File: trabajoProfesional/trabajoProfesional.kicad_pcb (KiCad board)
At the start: 2 copper layers, 190.8 x 81 mm, 115 parts, among them IC1 TS51231-QFNR, Q1 BSS84, U1 1501

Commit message: Editado el footprint que no teniamos, completando las ultimas placas
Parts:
- removed SensorPresion1: MS583730BA01-50, Connector_PinHeader_1.00mm:PinHeader_2x02_P1.00mm_Vertical_SMD
- removed U1: 1501, Connector_PinHeader_1.00mm:PinHeader_2x05_P1.00mm_Vertical_SMD
- added 4M0: 1501, Connector_PinHeader_2.54mm:PinHeader_2x05_P2.54mm_Vertical_SMD, F.Cu at (203.0, 117.8)
- added 4MS: MS583730BA01-50, Connector_PinHeader_2.54mm:PinHeader_2x02_P2.54mm_Vertical_SMD, B.Cu at (208.4, 112.4)
-  : renamed from TS80002; value Conn_01x20_Male -> 6TS8
- moved C11 59.2 mm to (-20.7, 109.5)
- moved Reset1 59.2 mm to (-6.29, 108.5)
- moved SDA1 59.2 mm to (-6.79, 114.0)
- moved TXCoil1 59.2 mm to (-12.3, 114.5)
- moved TXCoil2 59.2 mm to (-12.3, 108.5)
- moved C17 50.2 mm to (30.9, 154.4), turned to 180 degrees
- moved C16 28.1 mm to (30.1, 125.8), turned to 270 degrees
- moved C19 27.7 mm to (95.3, 109.6)
- moved R4 27.7 mm to (95.3, 112.5)
- moved C12 24.4 mm to (37.5, 122.2), turned to 270 degrees
- moved C18 23.6 mm to (40.6, 118.7), turned to 90 degrees
- moved C15 23.1 mm to (43.5, 123.0), turned to 90 degrees
- moved C10 23.0 mm to (33.3, 142.0)
- moved IC1 23.0 mm to (30.6, 148.8)
- moved R8 23.0 mm to (40.6, 125.8), turned to 270 degrees
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- renumbered Cin1 to 1C1, Cbst1 to 1C10, Cs2 to 1C2, Cout4 to 1C3, Cout3 to 1C4, Cc2 to 1C5, Cin2 to 1C6, Cc1 to 1C7, Cout1 to 1C8, Cout2 to 1C9, Coil1 to 1Coil1, Coil2 to 1Coil2, Lout1 to 1L1, R2fb1 to 1R1, Rmod_cfg1 to 1R2, R1fb1 to 1R3, RecpetorPotenciaInalambrica1 to 1RP, AdministracionBateria1 to 2AB, BatPositivo1 to 2B+, Cbat1 to 2C1, Cvin1 to 2C2, 3CH to 2CH, opt1 to 2D1, DbyPass1 to 2D2, batGND1 to 2GND, Q1 to 2Q1, RIPRGM1 to 2R1, Rstatus1 to 2R2, Riso_pd1 to 2R3, 3Vin to 2Vin, 3Vo to 2Vo, C4 to 3C1, C5 to 3C2, C2 to 3C3, C1 to 3C4, C3 to 3C5, D4 to 3D1, D1 to 3D2, D3 to 3D3, D2 to 3D4, DriverPotencia1 to 3DP, HV+1 to 3HV+, HV-1 to 3HV-, PiezoElectrico1 to 3PE, 2SN to 3SN, 10V1 to 3V10, 2Vin to 3Vin, C6 to 4C1, R1 to 4R1, R2 to 4R2, AlertDONE1 to 6Alert, Debug1 to 6Dg, SCL1 to 6SCL, Vcc5V1 to 6V5
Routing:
- net SDAPresion: track 23.1 -> 31.9 mm
- net SCLPresion: track 37.4 -> 28.7 mm
- net Net-(C6-Pad2): track 47.3 -> 38.9 mm
- net GND: track 387.3 -> 389.5 mm
- net /Bateria/Cargando: track 39.9 -> 42.1 mm
- net /Salida/SN1ONOFF: track 28.2 -> 26.6 mm
- net /Salida/SP1ONOFF: track 17.6 -> 18.4 mm
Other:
- outline, holes or cut-outs redrawn
- net class PIstasAnchas added: clearance 0.025, trace_width 1, via_dia 0.8, via_drill 0.4

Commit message: "placa 6 casi completa"
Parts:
- 6Alert, 6Dg, 6SCL, 6V5: moved to B.Cu
- moved 6Alert 14.7 mm to (41.4, 114.7)
- moved R5 14.1 mm to (67.1, 116.1), turned to 270 degrees
- moved 6SCL 8.85 mm to (49.9, 126.4)
- moved 6Dg 7.91 mm to (62.6, 117.4)
- moved 6V5 5.80 mm to (30.8, 114.2)
- moved C8 5.22 mm to (66.2, 109.1)
- moved D5 3.81 mm to (61.7, 111.7)
- moved C9 3.43 mm to (60.2, 107.2), turned to 0 degrees
- moved R6 2.78 mm to (56.3, 114.5)
- moved C13 2.48 mm to (54.4, 107.2)
- moved R7 2.37 mm to (56.3, 111.0)
- moved R3 0.92 mm to (60.2, 117.9)
- moved   0.82 mm to (49.4, 118.4)
- moved C7 0.75 mm to (49.0, 111.3)
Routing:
- net Net-(C13-Pad1): track 0.00 -> 17.3 mm
- net Net-(C8-Pad1): track 0.00 -> 14.3 mm
- net Net-(C7-Pad1): track 0.00 -> 12.7 mm
- net Net-(Debug1-Pad1): track 0.00 -> 11.8 mm, vias 0 -> 1
- net Net-(IC1-Pad1): track 0.00 -> 9.44 mm
- net Net-(SCL1-Pad1): track 0.00 -> 6.69 mm, vias 0 -> 1
- net Net-(C8-Pad2): track 0.00 -> 6.05 mm

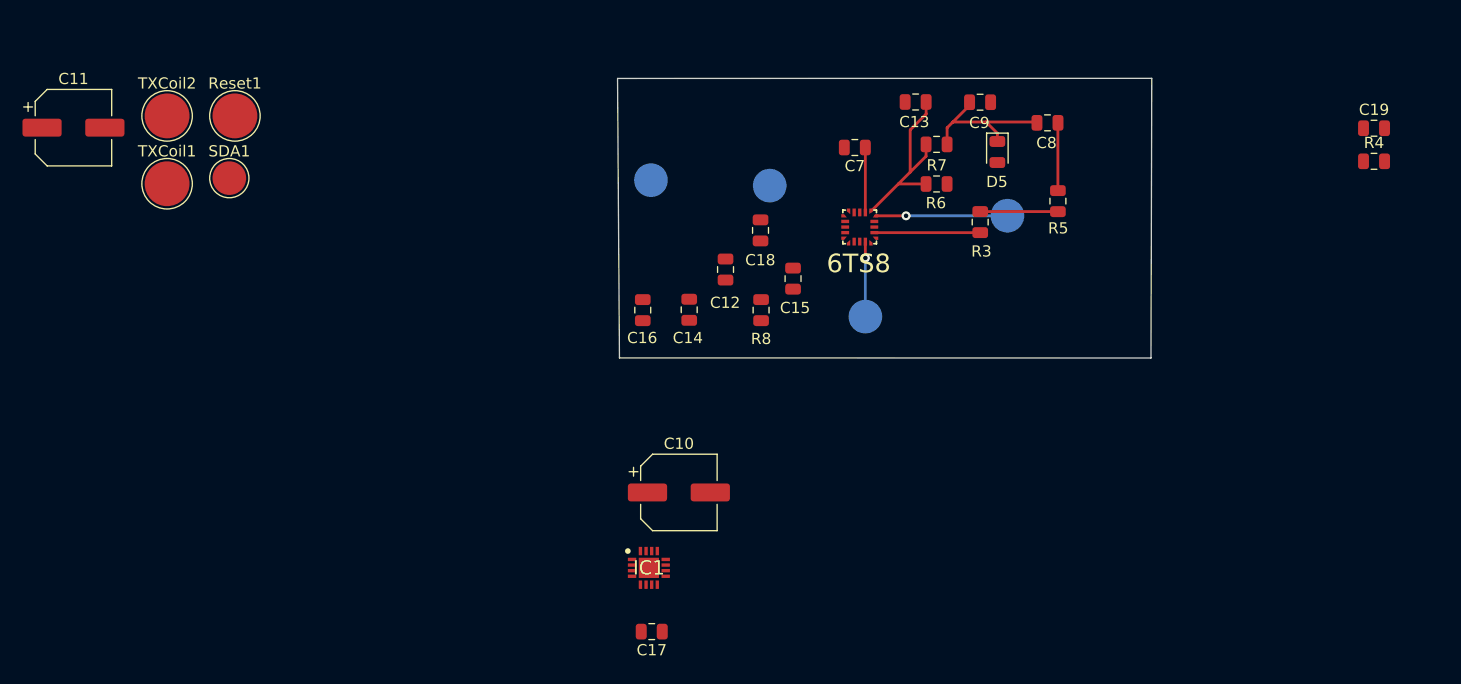
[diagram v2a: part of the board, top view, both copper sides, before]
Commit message: Se completo el centralizador, falta el step-up
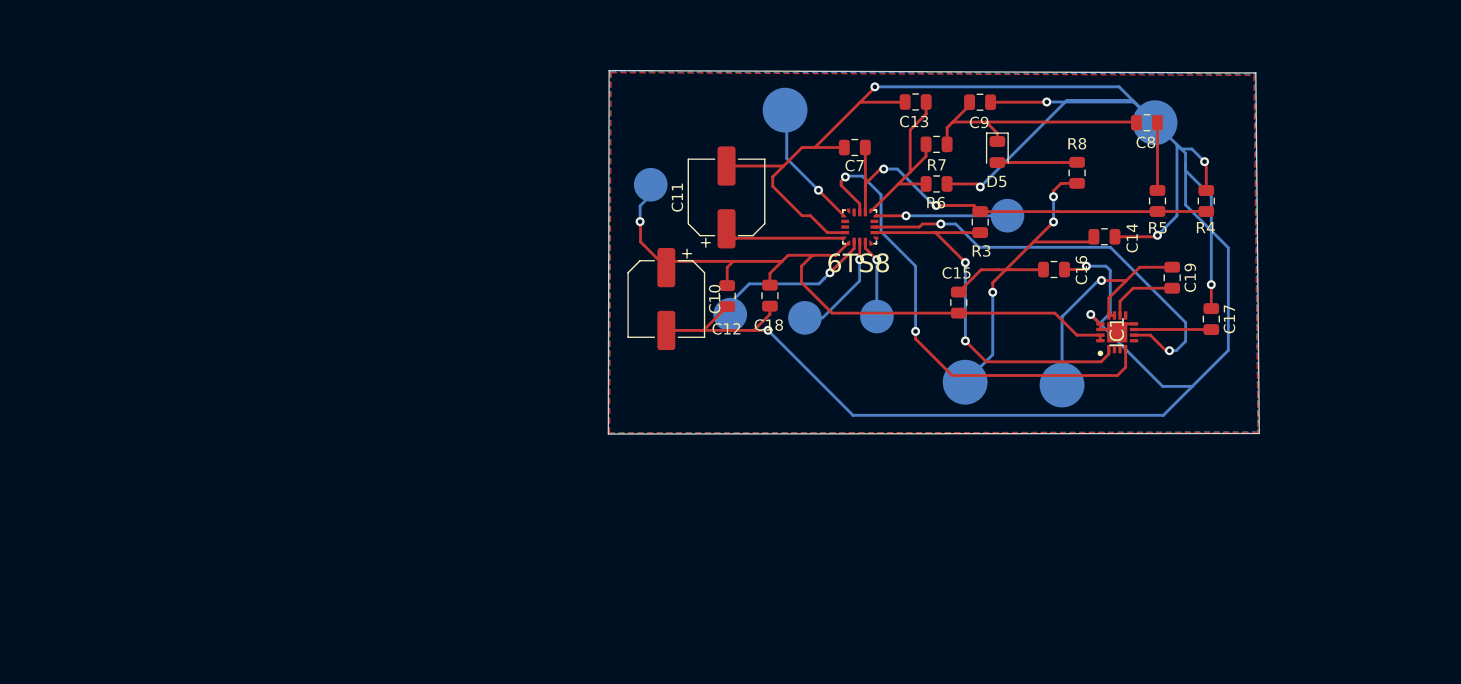
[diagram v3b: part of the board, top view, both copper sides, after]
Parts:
- added REF**: TestPoint_Pad_D4.0mm, TestPoint:TestPoint_Pad_D4.0mm, B.Cu at (75.8, 109.1)
- Reset1, SDA1, TXCoil1, TXCoil2: moved to B.Cu
- moved TXCoil1 81.8 mm to (67.5, 132.5)
- moved TXCoil2 75.0 mm to (58.8, 132.2)
- moved C11 58.6 mm to (37.5, 115.7), turned to 90 degrees
- moved C17 57.2 mm to (80.8, 126.6), turned to 270 degrees
- moved SDA1 52.8 mm to (44.5, 126.5)
- moved Reset1 49.1 mm to (42.8, 108.0)
- moved IC1 46.7 mm to (72.4, 127.8), turned to 90 degrees
- moved C14 37.6 mm to (71.2, 119.2), turned to 0 degrees
- moved C16 36.9 mm to (66.8, 122.2), turned to 0 degrees
- moved R8 30.7 mm to (68.8, 113.5), turned to 90 degrees
- moved C19 22.4 mm to (77.3, 122.9), turned to 270 degrees
- moved C10 17.3 mm to (32.2, 124.8), turned to 270 degrees
- moved R4 15.4 mm to (80.3, 116.0), turned to 90 degrees
- moved C15 14.9 mm to (58.3, 125.1), turned to 270 degrees
- moved 6Alert 12.0 mm to (37.9, 126.2)
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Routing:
- net GND: track 389.5 -> 629.2 mm, vias 21 -> 30
- net Net-(C10-Pad1): track 0.00 -> 63.0 mm, vias 0 -> 1
- net Net-(IC1-Pad4): track 0.00 -> 44.0 mm, vias 0 -> 2
- net Net-(IC1-Pad6): track 0.00 -> 38.7 mm, vias 0 -> 2
- net Net-(C14-Pad1): track 0.00 -> 36.7 mm, vias 0 -> 3
- net Net-(C7-Pad1): track 12.7 -> 39.1 mm, vias 0 -> 2
- net Net-(IC1-Pad1): track 9.44 -> 34.6 mm, vias 0 -> 2
- net Net-(C19-Pad1): track 0.00 -> 21.9 mm, vias 0 -> 1
- net Net-(AlertDONE1-Pad1): track 0.00 -> 14.7 mm, vias 0 -> 1
- net Net-(Reset1-Pad1): track 0.00 -> 11.6 mm, vias 0 -> 1
- net Net-(C11-Pad1): track 0.00 -> 10.8 mm
- net Net-(SDA1-Pad1): track 0.00 -> 9.75 mm, vias 0 -> 1
- net Net-(C8-Pad1): track 14.3 -> 23.1 mm
- net Net-(D5-Pad2): track 0.00 -> 7.12 mm
- net Net-(C17-Pad2): track 0.00 -> 6.89 mm
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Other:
- board size 190.8 x 81 mm -> 191.6 x 87.7 mm

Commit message: terminadas las 8 placas modulares. Para mandar a imprimir!
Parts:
- added 7C1: 10u, Capacitor_SMD:C_0805_2012Metric, F.Cu at (123.9, 24.8)
- added 7C2: 1u, Capacitor_SMD:C_0805_2012Metric, F.Cu at (156.1, 25.4)
- added 7C3: 10u, Capacitor_SMD:C_0805_2012Metric, F.Cu at (138.6, 33.8)
- added 7C4: 1u, Capacitor_SMD:C_0805_2012Metric, F.Cu at (149.6, 34.9)
- added 7C5: 1u, Capacitor_SMD:C_0805_2012Metric, F.Cu at (162.6, 37.3)
- added 7DIO: DIO6605BFN8, DIO6605BFN8:SON50P300X200X80-9N-D, F.Cu at (130.9, 32.5)
- added 7GND: TestPoint_Pad_D4.0mm, TestPoint:TestPoint_Pad_D4.0mm, B.Cu at (145.4, 36.7)
- added 7L1: 4.7u, Inductor_SMD:L_0603_1608Metric_Pad1.05x0.95mm_HandSolder, F.Cu at (119.5, 32.5)
- added 7TPS: TPS60402DBVR, TPS60402DBVR:SOT95P280X145-5N, F.Cu at (156.1, 33.3)
- added 7V-5: TestPoint_Pad_D4.0mm, TestPoint:TestPoint_Pad_D4.0mm, B.Cu at (161.8, 24.9)
- added 7V3.3: TestPoint_Pad_D4.0mm, TestPoint:TestPoint_Pad_D4.0mm, B.Cu at (122.3, 37.1)
- added 7V5: TestPoint_Pad_D4.0mm, TestPoint:TestPoint_Pad_D4.0mm, B.Cu at (128.4, 25.3)
- added 8MS: , footprints:MS583730BA01-50, B.Cu at (45.0, 27.5)
- added 8OUT: , Connector_PinHeader_2.54mm:PinHeader_2x02_P2.54mm_Vertical_SMD, F.Cu at (57.5, 27.7)
- 6TS8: renamed from  ; value 6TS8 -> (none)
- renumbered 2SP to 3SP, 4M0 to 4MO, 5C22 to 5C1, 5C20 to 5C2, 5C21 to 5C3, 5C25 to 5C4, 5C24 to 5C5, 5C23 to 5C6, 5D8 to 5D1, 5D6 to 5D2, 5D7 to 5D3, 5D10 to 5D4, 5D11 to 5D6, 5D9 to 5D7, 5V- to 5HV-, 5inA to 5InA, 5inB to 5InB, 5R9 to 5R1, C13 to 6C1, C15 to 6C10, C16 to 6C11, C19 to 6C12, C17 to 6C13, C9 to 6C2, C8 to 6C3, C7 to 6C4, C11 to 6C5, C14 to 6C6, C10 to 6C7, C12 to 6C8, C18 to 6C9, TXCoil1 to 6Coil1, TXCoil2 to 6Coil2, D5 to 6D1, 6Dg to 6Debug, REF** to 6GND, R7 to 6R1, R6 to 6R2, R8 to 6R3, R5 to 6R4, R4 to 6R5, Reset1 to 6Reset, SDA1 to 6SDA, IC1 to 6TS51
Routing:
- net GND: track 629.2 -> 727.0 mm, vias 30 -> 35
- net (no net): track 0.00 -> 61.1 mm, vias 0 -> 4
- net /StepUpStepDown/Vin3.3: track 0.00 -> 58.4 mm, vias 0 -> 1
- net /StepUpStepDown/+5Vout: track 0.00 -> 38.8 mm, vias 0 -> 1
- net /StepUpStepDown/-5VOut: track 0.00 -> 16.1 mm, vias 0 -> 1
- net Net-(IC3-Pad4): track 0.00 -> 10.0 mm
- net Net-(C29-Pad1): track 0.00 -> 9.54 mm
- net Net-(C29-Pad2): track 0.00 -> 9.41 mm
- added copper zone on B.Cu, net (none)
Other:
- board size 191.6 x 87.7 mm -> 191.6 x 115.6 mm
- board text added: "Adaptador"
- board text added: "Base Carga"
- board text added: "Centralizador"
- board text added: "Step Up Down"

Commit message: se unifica todo
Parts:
- moved 8MS 121.8 mm to (148.3, 92.0), turned to 180 degrees
- moved 7L1 109.1 mm to (167.7, 130.3), turned to 0 degrees
- moved 7C1 107.3 mm to (159.9, 125.9), turned to 0 degrees
- moved 4CH 106.5 mm to (126.8, 61.5), turned to 180 degrees
- moved 7V3.3 103.3 mm to (172.3, 127.5), turned to 90 degrees
- moved 4R1 101.9 mm to (127.5, 64.6), turned to 90 degrees
- moved 7V5 101.3 mm to (160.4, 121.3), turned to 90 degrees
- moved 8OUT 101.2 mm to (135.8, 91.8), turned to 180 degrees
- moved 1C4 97.5 mm to (116.6, 64.2)
- moved 1GND 97.5 mm to (118.8, 76.4)
- moved 1C1 97.5 mm to (101.3, 60.2)
- moved 1C3 97.5 mm to (111.5, 63.4)
- moved 1C5 97.5 mm to (118.1, 65.2)
- moved 1C7 97.5 mm to (100.7, 68.5)
- moved 1C8 97.5 mm to (107.3, 68.4)
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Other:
- board size 191.6 x 115.6 mm -> 100.5 x 78.1 mm

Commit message: se agregan lineas
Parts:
-  : renamed from 6TS8
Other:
- board text added: ". _ . _ . _ . _ . _ ."
- board text added: ". _ . _ . _ . _ . _ . _ . _ . _ . _ . _ . _ . _ . _"
- board text added: ". _ . _ . _ . _ . _ . _ . _ . _ . _ . _ . _ . _ . _ . _ ."
- board text added: "6TS8"
- board text added: "_ . _ . _ . _"
- board text added: "_ . _ . _ . _ . _"
- board text added: "_ . _ . _ . _ . _ ."
- board text added: "_ . _ . _ . _ . _ . _"
- board text added: "_ . _ . _ . _ . _ . _ ."
- board text added: "_ . _ . _ . _ . _ . _ . _ ."
- board text added: "_ . _ . _ . _ . _ . _ . _ . _ ."
- board text added: "_ . _ . _ . _ . _ . _ . _ . _ . _ . _"
